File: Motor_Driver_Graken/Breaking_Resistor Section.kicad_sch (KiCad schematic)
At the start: 5 parts, among them Q7 Q_NMOS_DGS, U11 1ED3121MC12HXUMA1

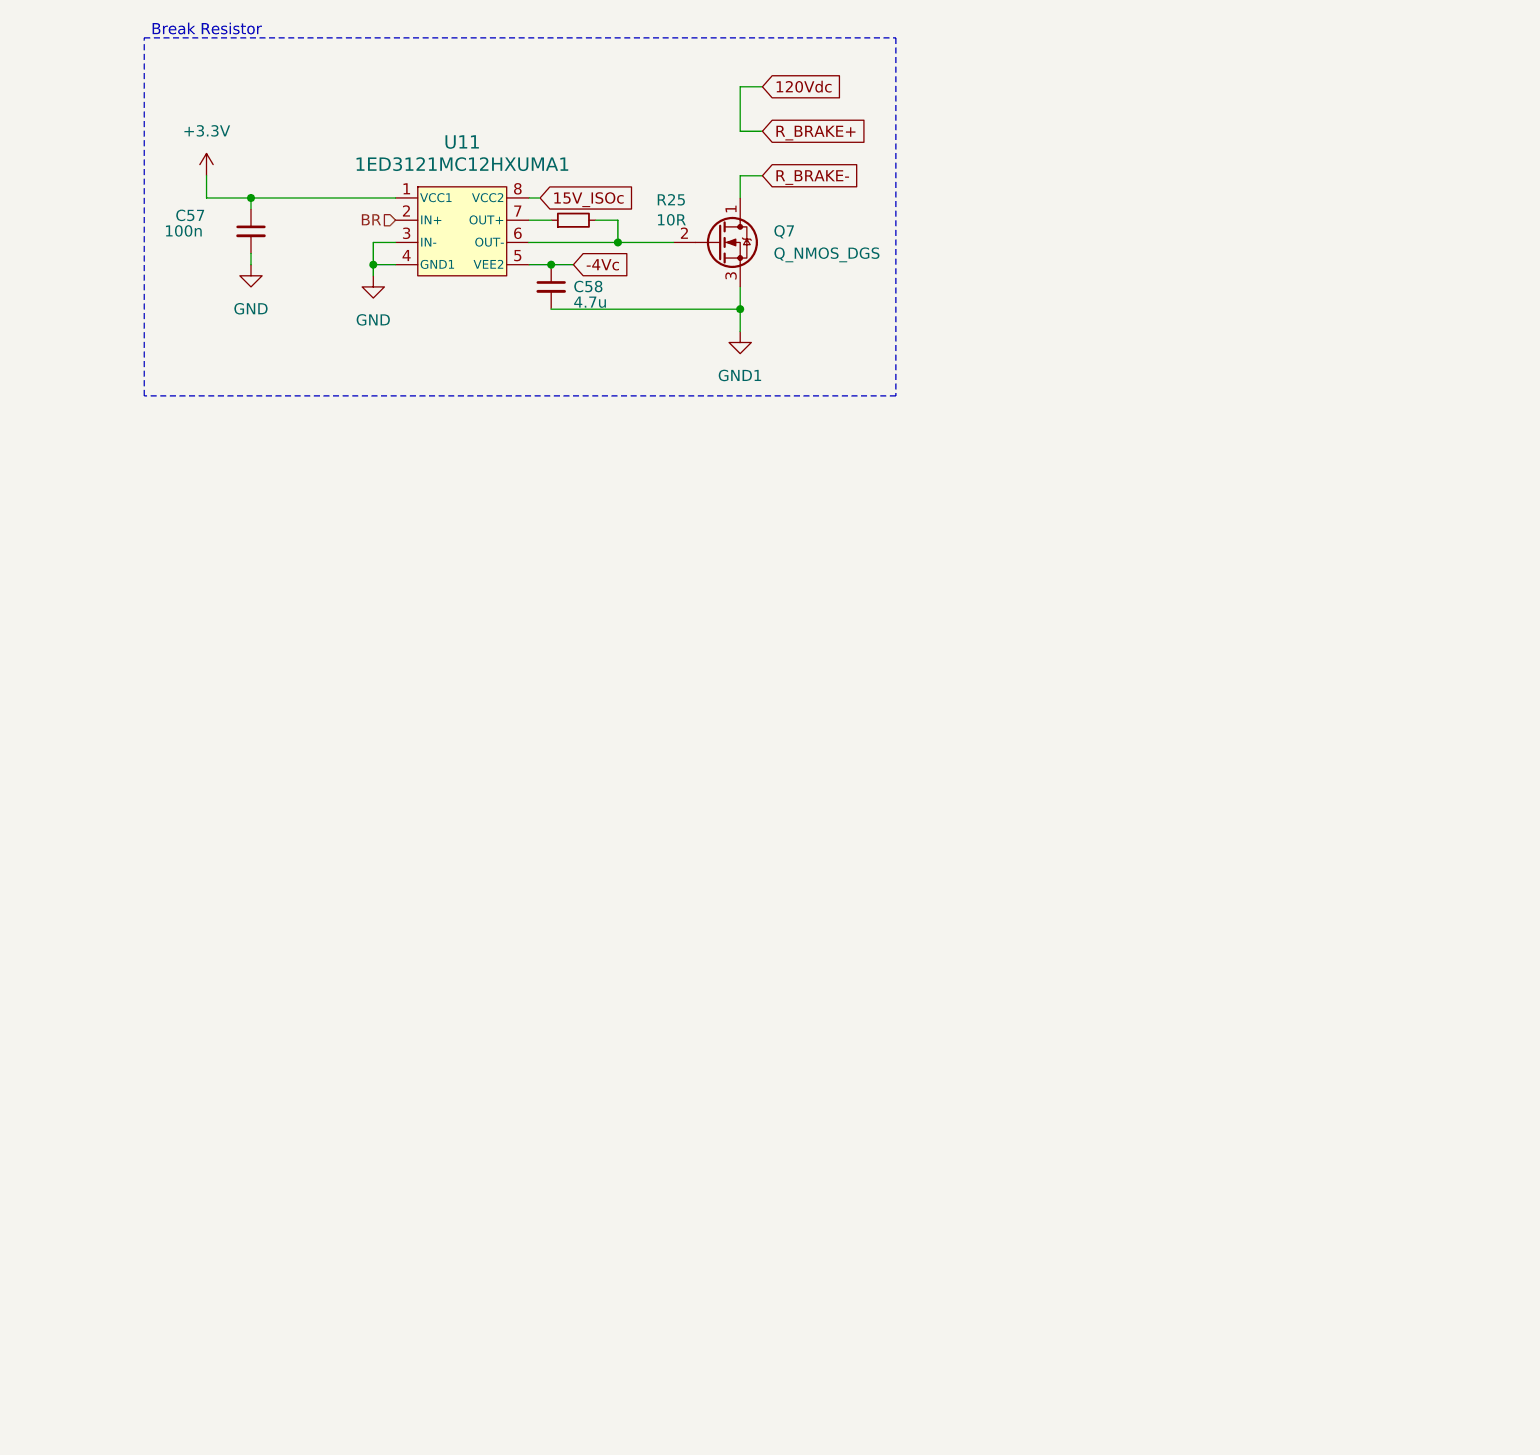
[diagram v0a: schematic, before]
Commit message: Break Resistor Section
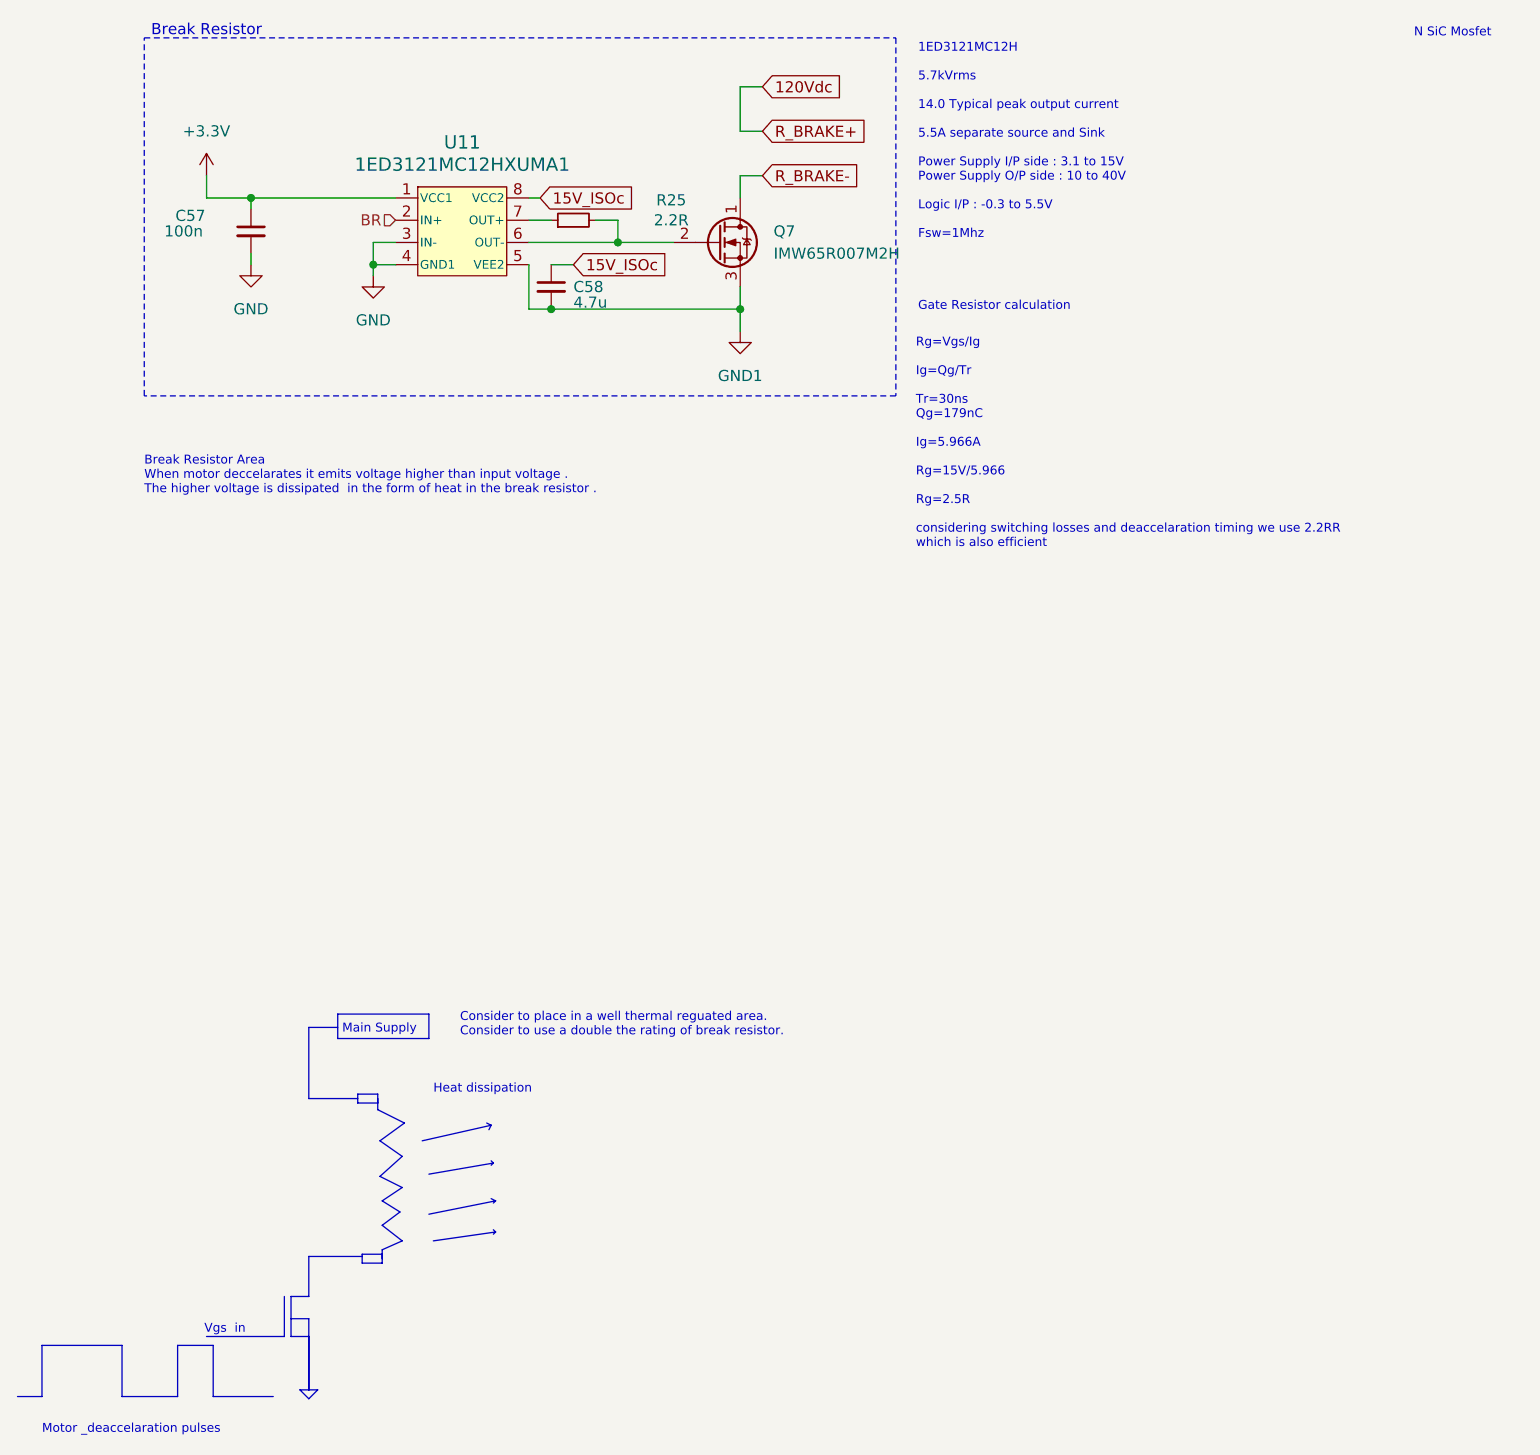
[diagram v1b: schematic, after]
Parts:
- Q7: value Q_NMOS_DGS -> IMW65R007M2H
- R25: value 10R -> 2.2R
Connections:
- net 15V_ISOc: now also C58.1
- net GND1: now also U11.5 (VEE2)
- removed net -4Vc: C58.1, U11.5 (VEE2)
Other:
- note added: "1ED3121MC12H 5.7kVrms 14.0 Typical peak output current 5.5A separate source and Sink Power Supply I/P side : 3.1 to 15V Power Supply O/P side : 10 to 40V Logic I/P : -0.3 to 5.5V Fsw=1Mhz"
- note added: "Break Resistor Area When motor deccelarates it emits voltage higher than input voltage . The higher voltage is dissipated in the form of heat in the break resistor ."
- note added: "Consider to place in a well thermal reguated area. Consider to use a double the rating of break resistor."
- note added: "Gate Resistor calculation"
- note added: "Heat dissipation"
- note added: "Main Supply"
- note added: "Motor _deaccelaration pulses"
- note added: "N SiC Mosfet"
- note added: "Rg=Vgs/Ig Ig=Qg/Tr Tr=30ns Qg=179nC Ig=5.966A Rg=15V/5.966 Rg=2.5R considering switching losses and deaccelaration timing we use 2.2RR which is also efficient"
- note added: "Vgs in"

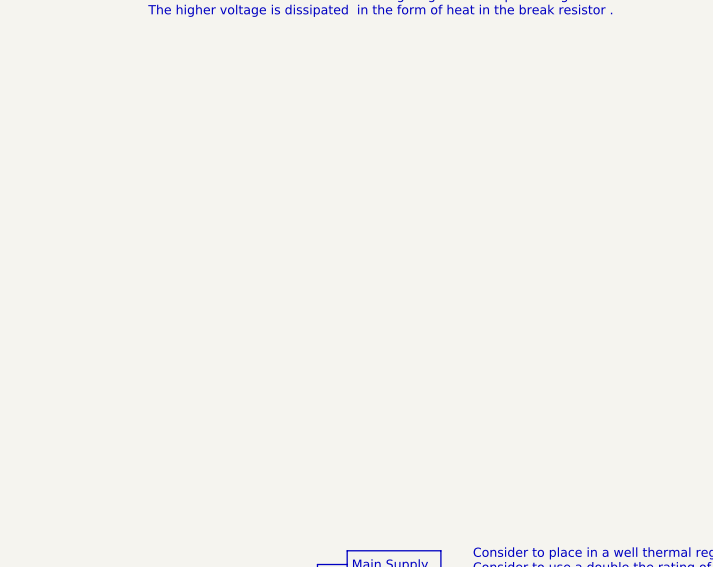
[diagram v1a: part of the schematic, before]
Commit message: adding simulation results
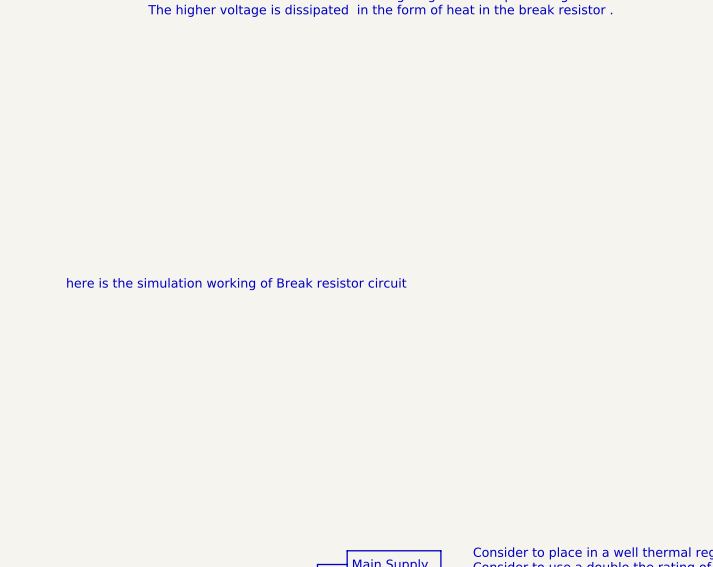
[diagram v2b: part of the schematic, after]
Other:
- note added: "here is the simulation working of Break resistor circuit"

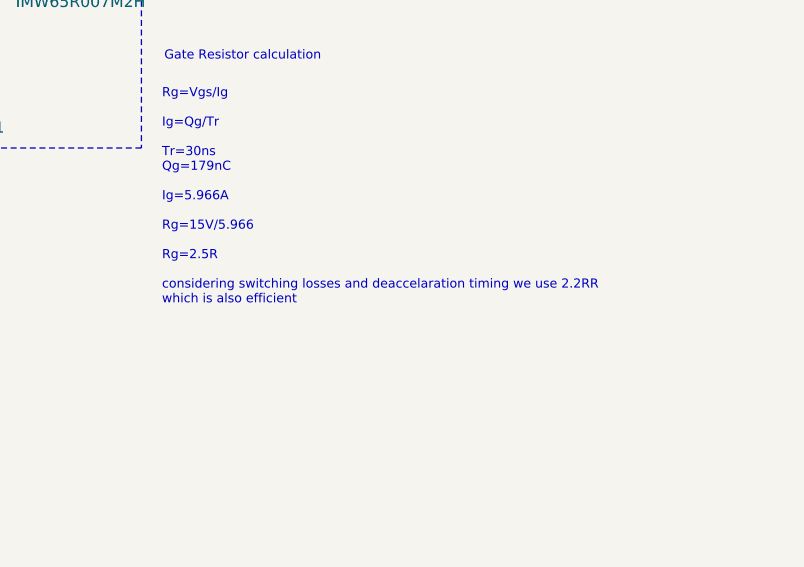
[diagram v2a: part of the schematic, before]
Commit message: Break resistor and IC details
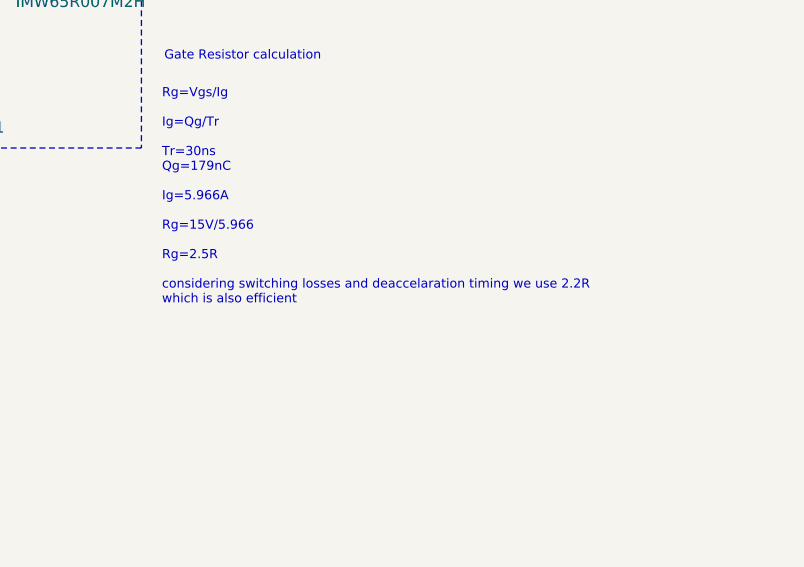
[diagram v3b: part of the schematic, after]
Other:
- note added: "Rg=Vgs/Ig Ig=Qg/Tr Tr=30ns Qg=179nC Ig=5.966A Rg=15V/5.966 Rg=2.5R considering switching losses and deaccelaration timing we use 2.2R which is also efficient"
- note removed: "Rg=Vgs/Ig Ig=Qg/Tr Tr=30ns Qg=179nC Ig=5.966A Rg=15V/5.966 Rg=2.5R considering switching losses and deaccelaration timing we use 2.2RR which is also efficient"
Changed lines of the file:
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@@
 		)
 	)
-	(text "Rg=Vgs/Ig\n\nIg=Qg/Tr\n\nTr=30ns\nQg=179nC\n\nIg=5.966A\n\nRg=15V/5.966\n\nRg=2.5R\n\nconsidering switching losses and deaccelaration timing we use 2.2RR \nwhich is also efficient\n\n\n"
+	(text "Rg=Vgs/Ig\n\nIg=Qg/Tr\n\nTr=30ns\nQg=179nC\n\nIg=5.966A\n\nRg=15V/5.966\n\nRg=2.5R\n\nconsidering switching losses and deaccelaration timing we use 2.2R \nwhich is also efficient\n\n\n"
 		(exclude_from_sim no)
 		(at 117.856 79.248 0)
